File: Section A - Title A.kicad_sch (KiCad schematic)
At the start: 9 parts, among them J5 THD-02-R, J6 Conn_01x22_Female, J7 690-019-298-412, U1 RT9742SNGV

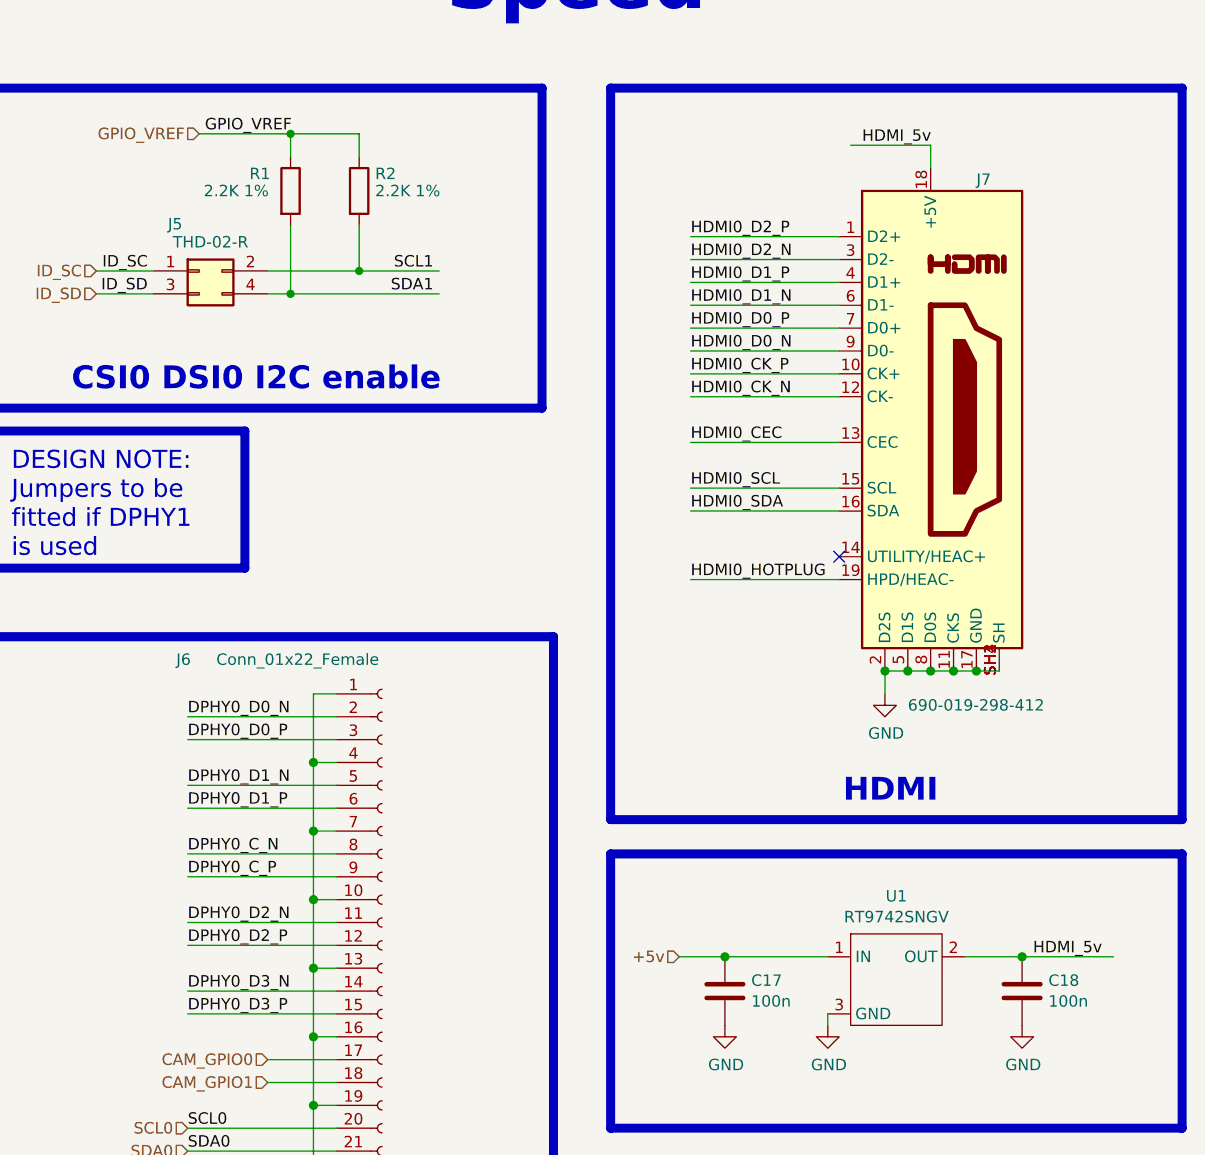
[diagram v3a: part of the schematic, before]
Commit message: Sheet name edit and changed to net labels
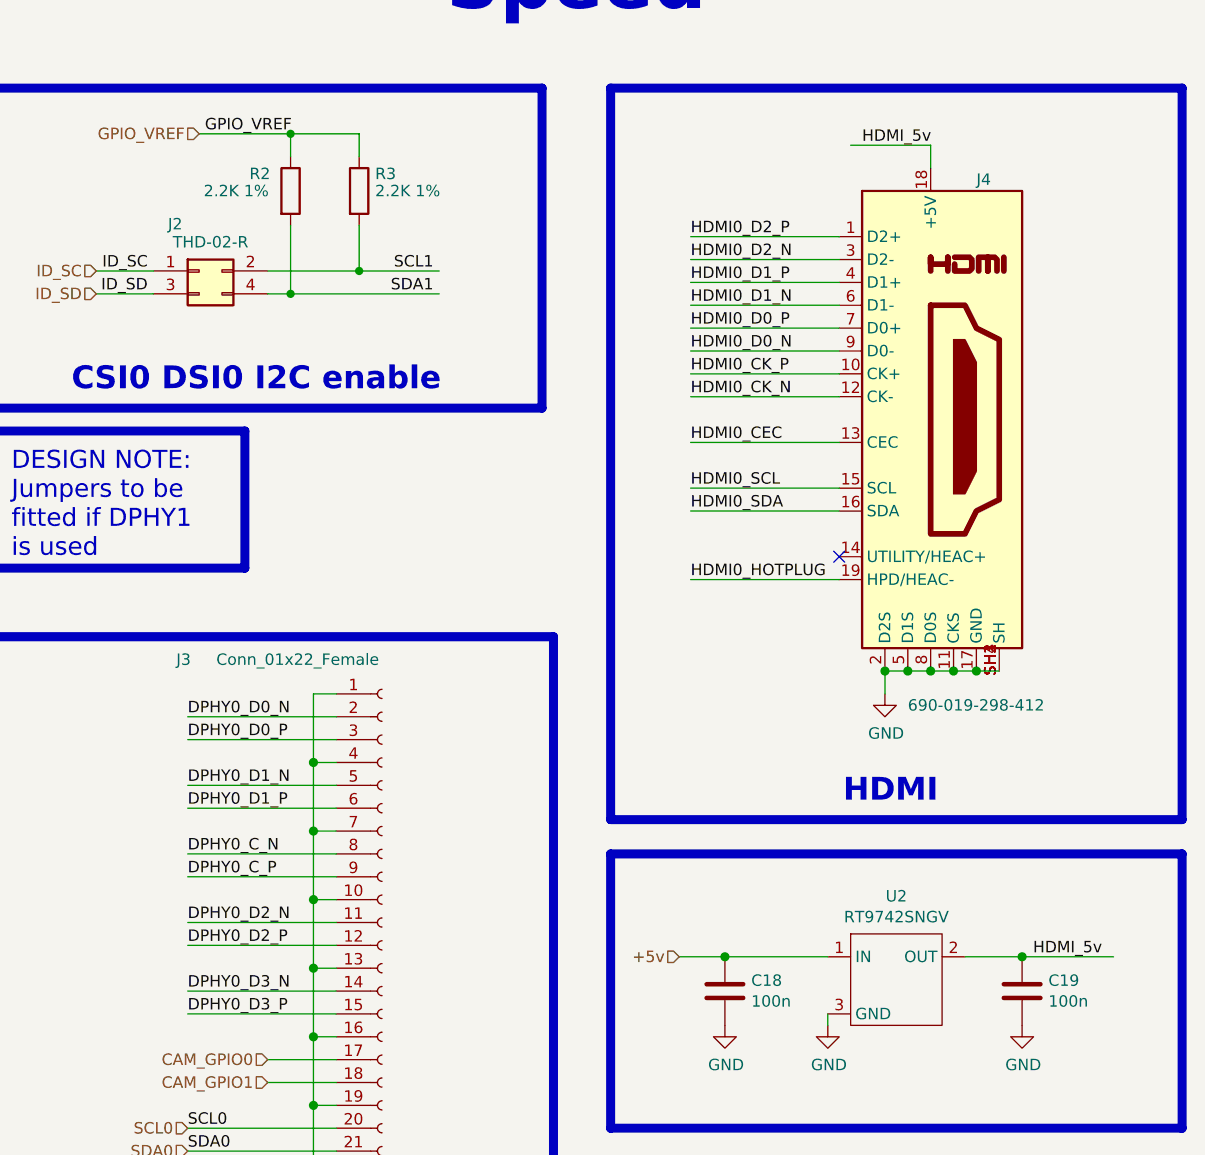
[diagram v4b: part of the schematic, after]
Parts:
- renumbered C17 to C18, C18 to C19, J5 to J2, J6 to J3, J7 to J4, R1 to R2, R2 to R3, U1 to U2
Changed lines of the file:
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@@
 		(on_board yes)
 		(dnp no)
-		(property "Reference" "#PWR011"
+		(property "Reference" "#PWR010"
 			(at 242.57 110.49 0)
 			(effects
@@
 			(project "CM5 Nas"
 				(path "/0650c7a8-acba-429c-9f8e-eec0baf0bc1c/fede4c36-00cc-4d3d-b71c-5243ba232202/7d5a1283-086b-46b0-8df7-a9850521fb5e"
-					(reference "#PWR011")
+					(reference "#PWR010")
 					(unit 1)
 				)
@@
 		(on_board yes)
 		(dnp no)
-		(property "Reference" "#PWR07"
+		(property "Reference" "#PWR06"
 			(at 104.14 166.37 0)
 			(effects
@@
 			(project "CM5 Nas"
 				(path "/0650c7a8-acba-429c-9f8e-eec0baf0bc1c/fede4c36-00cc-4d3d-b71c-5243ba232202/7d5a1283-086b-46b0-8df7-a9850521fb5e"
-					(reference "#PWR07")
+					(reference "#PWR06")
 					(unit 1)
 				)
@@
 		(on_board yes)
 		(dnp no)
-		(property "Reference" "#PWR06"
+		(property "Reference" "#PWR05"
 			(at 38.1 166.37 0)
 			(effects
@@
 			(project "CM5 Nas"
 				(path "/0650c7a8-acba-429c-9f8e-eec0baf0bc1c/fede4c36-00cc-4d3d-b71c-5243ba232202/7d5a1283-086b-46b0-8df7-a9850521fb5e"
-					(reference "#PWR06")
+					(reference "#PWR05")
 					(unit 1)
 				)
@@
 		(on_board yes)
 		(dnp no)
-		(property "Reference" "#PWR08"
+		(property "Reference" "#PWR07"
 			(at 179.07 165.1 0)
 			(effects
@@
 			(project "CM5 Nas"
 				(path "/0650c7a8-acba-429c-9f8e-eec0baf0bc1c/fede4c36-00cc-4d3d-b71c-5243ba232202/7d5a1283-086b-46b0-8df7-a9850521fb5e"
-					(reference "#PWR08")
+					(reference "#PWR07")
 					(unit 1)
 				)
@@
 		(on_board yes)
 		(dnp no)
-		(property "Reference" "R1"
+		(property "Reference" "R2"
 			(at 171.958 46.355 0)
 			(effects
@@
 			(project "CM5 Nas"
 				(path "/0650c7a8-acba-429c-9f8e-eec0baf0bc1c/fede4c36-00cc-4d3d-b71c-5243ba232202/7d5a1283-086b-46b0-8df7-a9850521fb5e"
-					(reference "R1")
+					(reference "R2")
 					(unit 1)
 				)
@@
 		(on_board yes)
 		(dnp no)
-		(property "Reference" "R2"
+		(property "Reference" "R3"
 			(at 185.928 46.355 0)
 			(effects
@@
 			(project "CM5 Nas"
 				(path "/0650c7a8-acba-429c-9f8e-eec0baf0bc1c/fede4c36-00cc-4d3d-b71c-5243ba232202/7d5a1283-086b-46b0-8df7-a9850521fb5e"
-					(reference "R2")
+					(reference "R3")
 					(unit 1)
 				)
@@
 		(on_board yes)
 		(dnp no)
-		(property "Reference" "J6"
+		(property "Reference" "J3"
 			(at 163.83 100.33 0)
 			(effects
@@
 			(project "CM5 Nas"
 				(path "/0650c7a8-acba-429c-9f8e-eec0baf0bc1c/fede4c36-00cc-4d3d-b71c-5243ba232202/7d5a1283-086b-46b0-8df7-a9850521fb5e"
-					(reference "J6")
+					(reference "J3")
 					(unit 1)
 				)
@@
 		(on_board yes)
 		(dnp no)
-		(property "Reference" "J7"
+		(property "Reference" "J4"
 			(at 252.73 46.99 0)
 			(effects
@@
 			(project "CM5 Nas"
 				(path "/0650c7a8-acba-429c-9f8e-eec0baf0bc1c/fede4c36-00cc-4d3d-b71c-5243ba232202/7d5a1283-086b-46b0-8df7-a9850521fb5e"
-					(reference "J7")
+					(reference "J4")
 					(unit 1)
 				)
@@
 		(on_board yes)
 		(dnp no)
-		(property "Reference" "C18"
+		(property "Reference" "C19"
 			(at 260.731 135.9916 0)
 			(effects
@@
 			(project "CM5 Nas"
 				(path "/0650c7a8-acba-429c-9f8e-eec0baf0bc1c/fede4c36-00cc-4d3d-b71c-5243ba232202/7d5a1283-086b-46b0-8df7-a9850521fb5e"
-					(reference "C18")
+					(reference "C19")
 					(unit 1)
 				)
@@
 		(on_board yes)
 		(dnp no)
-		(property "Reference" "C17"
+		(property "Reference" "C18"
 			(at 227.711 135.9916 0)
 			(effects
@@
 			(project "CM5 Nas"
 				(path "/0650c7a8-acba-429c-9f8e-eec0baf0bc1c/fede4c36-00cc-4d3d-b71c-5243ba232202/7d5a1283-086b-46b0-8df7-a9850521fb5e"
-					(reference "C17")
+					(reference "C18")
 					(unit 1)
 				)
@@
 		(on_board yes)
 		(dnp no)
-		(property "Reference" "U1"
+		(property "Reference" "U2"
 			(at 243.84 126.619 0)
 			(effects
@@
 			(project "CM5 Nas"
 				(path "/0650c7a8-acba-429c-9f8e-eec0baf0bc1c/fede4c36-00cc-4d3d-b71c-5243ba232202/7d5a1283-086b-46b0-8df7-a9850521fb5e"
-					(reference "U1")
+					(reference "U2")
 					(unit 1)
 				)
@@
 		(on_board yes)
 		(dnp no)
-		(property "Reference" "#PWR012"
+		(property "Reference" "#PWR011"
 			(at 257.81 147.32 0)
 			(effects
@@
 			(project "CM5 Nas"
 				(path "/0650c7a8-acba-429c-9f8e-eec0baf0bc1c/fede4c36-00cc-4d3d-b71c-5243ba232202/7d5a1283-086b-46b0-8df7-a9850521fb5e"
-					(reference "#PWR012")
+					(reference "#PWR011")
 					(unit 1)
 				)
@@
 		(on_board yes)
 		(dnp no)
-		(property "Reference" "#PWR09"
+		(property "Reference" "#PWR08"
 			(at 224.79 147.32 0)
 			(effects
@@
 			(project "CM5 Nas"
 				(path "/0650c7a8-acba-429c-9f8e-eec0baf0bc1c/fede4c36-00cc-4d3d-b71c-5243ba232202/7d5a1283-086b-46b0-8df7-a9850521fb5e"
-					(reference "#PWR09")
+					(reference "#PWR08")
 					(unit 1)
 				)
@@
 		(on_board yes)
 		(dnp no)
-		(property "Reference" "#PWR010"
+		(property "Reference" "#PWR09"
 			(at 236.22 147.32 0)
 			(effects
@@
 			(project "CM5 Nas"
 				(path "/0650c7a8-acba-429c-9f8e-eec0baf0bc1c/fede4c36-00cc-4d3d-b71c-5243ba232202/7d5a1283-086b-46b0-8df7-a9850521fb5e"
-					(reference "#PWR010")
+					(reference "#PWR09")
 					(unit 1)
 				)
@@
 		(on_board yes)
 		(dnp no)
-		(property "Reference" "J5"
+		(property "Reference" "J2"
 			(at 163.703 51.943 0)
 			(effects
@@
 			(project "CM5 Nas"
 				(path "/0650c7a8-acba-429c-9f8e-eec0baf0bc1c/fede4c36-00cc-4d3d-b71c-5243ba232202/7d5a1283-086b-46b0-8df7-a9850521fb5e"
-					(reference "J5")
+					(reference "J2")
 					(unit 1)
 				)

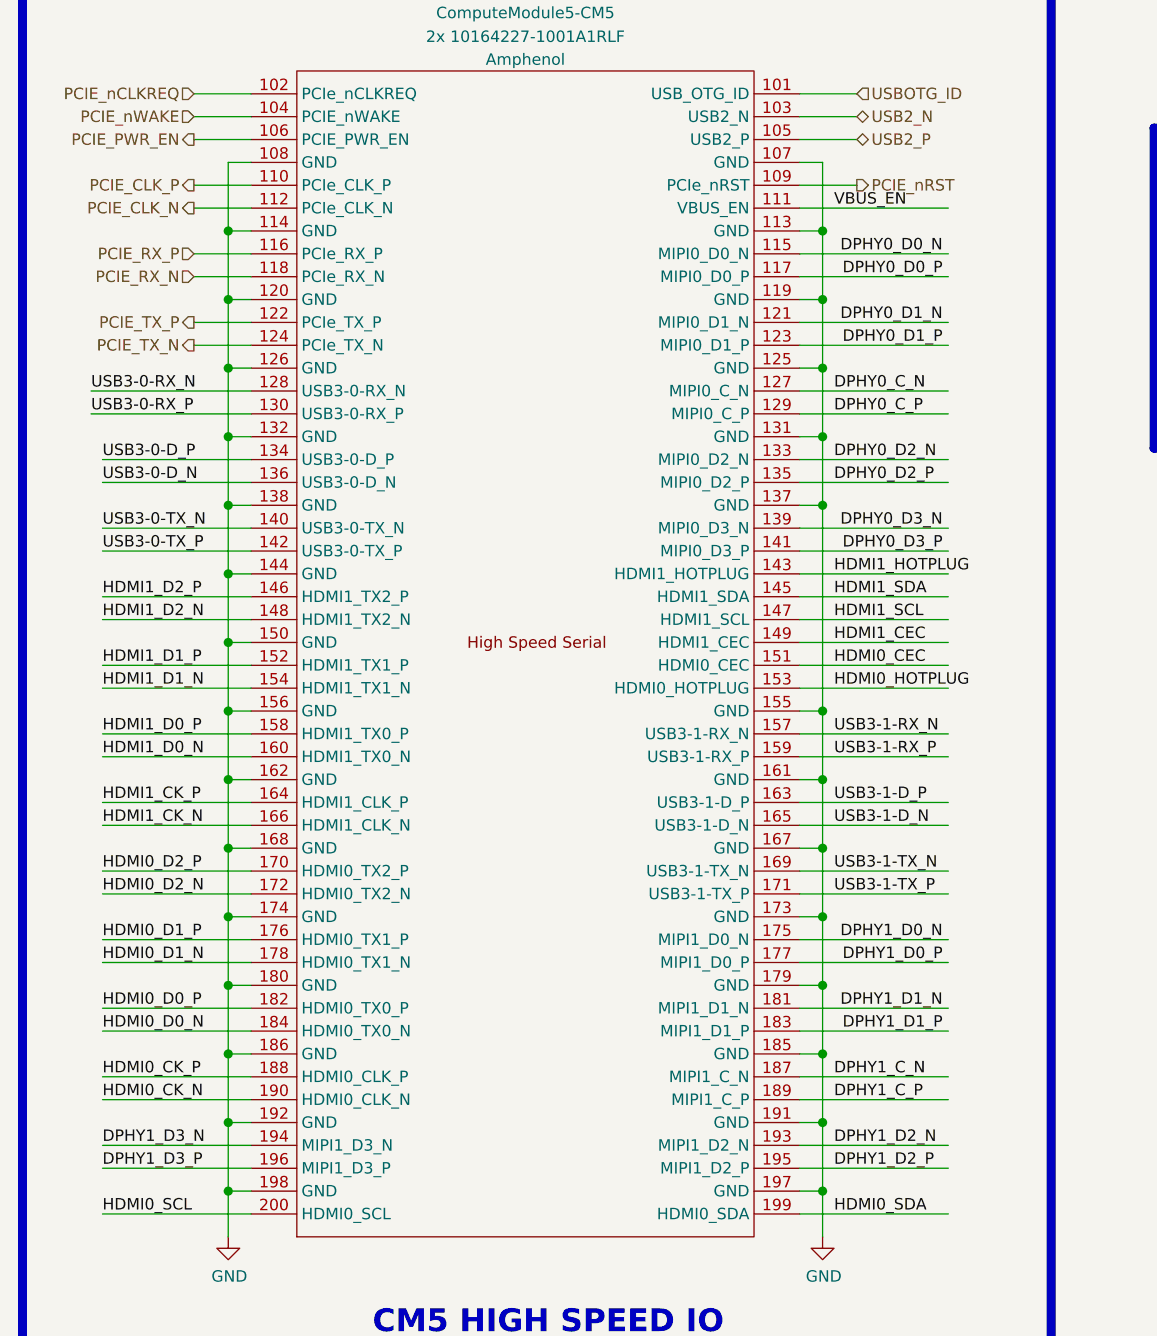
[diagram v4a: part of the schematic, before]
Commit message: Notation changed on M.2 Sheet
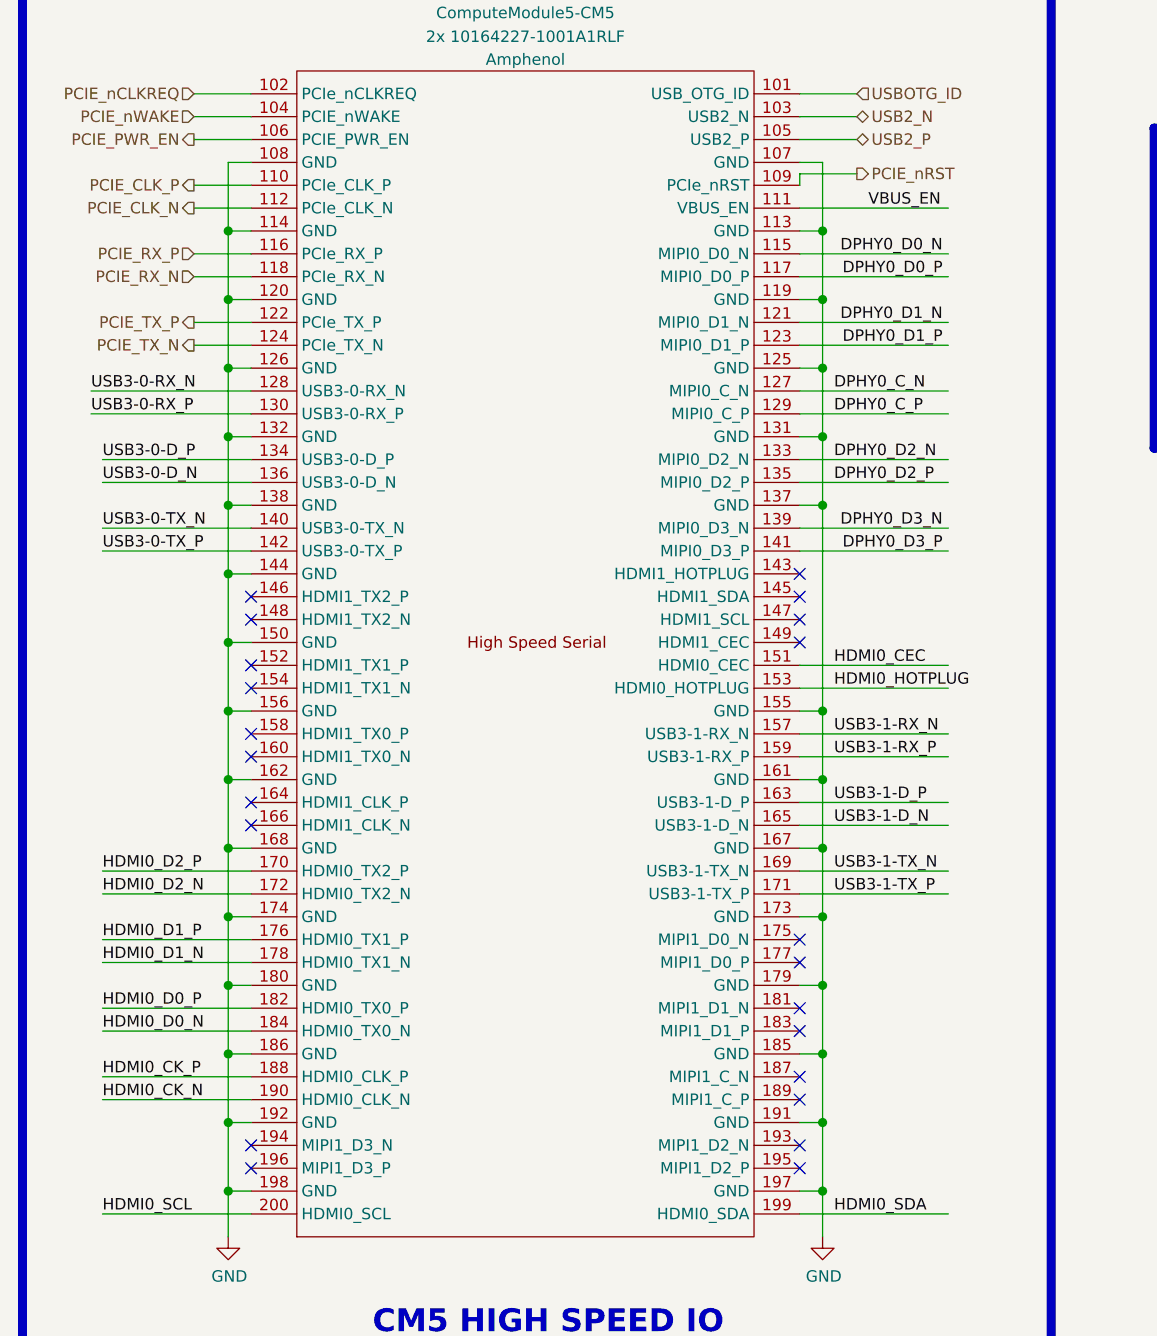
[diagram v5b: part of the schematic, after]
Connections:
- net DPHY1_C_N: no longer names the net of Module1.187 (MIPI1_C_N)
- net DPHY1_C_P: no longer names the net of Module1.189 (MIPI1_C_P)
- net DPHY1_D0_N: no longer names the net of Module1.175 (MIPI1_D0_N)
- net DPHY1_D0_P: no longer names the net of Module1.177 (MIPI1_D0_P)
- net DPHY1_D1_N: no longer names the net of Module1.181 (MIPI1_D1_N)
- net DPHY1_D1_P: no longer names the net of Module1.183 (MIPI1_D1_P)
- net DPHY1_D2_N: no longer names the net of Module1.193 (MIPI1_D2_N)
- net DPHY1_D2_P: no longer names the net of Module1.195 (MIPI1_D2_P)
- net DPHY1_D3_N: no longer names the net of Module1.194 (MIPI1_D3_N)
- net DPHY1_D3_P: no longer names the net of Module1.196 (MIPI1_D3_P)
- net HDMI1_CEC: no longer names the net of Module1.149 (HDMI1_CEC)
- net HDMI1_CK_N: no longer names the net of Module1.166 (HDMI1_CLK_N)
- net HDMI1_CK_P: no longer names the net of Module1.164 (HDMI1_CLK_P)
- net HDMI1_D0_N: no longer names the net of Module1.160 (HDMI1_TX0_N)
- net HDMI1_D0_P: no longer names the net of Module1.158 (HDMI1_TX0_P)
- net HDMI1_D1_N: no longer names the net of Module1.154 (HDMI1_TX1_N)
- net HDMI1_D1_P: no longer names the net of Module1.152 (HDMI1_TX1_P)
- net HDMI1_D2_N: no longer names the net of Module1.148 (HDMI1_TX2_N)
- net HDMI1_D2_P: no longer names the net of Module1.146 (HDMI1_TX2_P)
- net HDMI1_HOTPLUG: no longer names the net of Module1.143 (HDMI1_HOTPLUG)
- net HDMI1_SCL: no longer names the net of Module1.147 (HDMI1_SCL)
- net HDMI1_SDA: no longer names the net of Module1.145 (HDMI1_SDA)
- no-connect marks 1 -> 23
